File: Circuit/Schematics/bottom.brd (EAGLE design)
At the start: 38.1 x 38.1 mm, 52 parts, among them IC1 LM2936MP-3.3, Y1 16 Mhz, Y2 16 Mhz

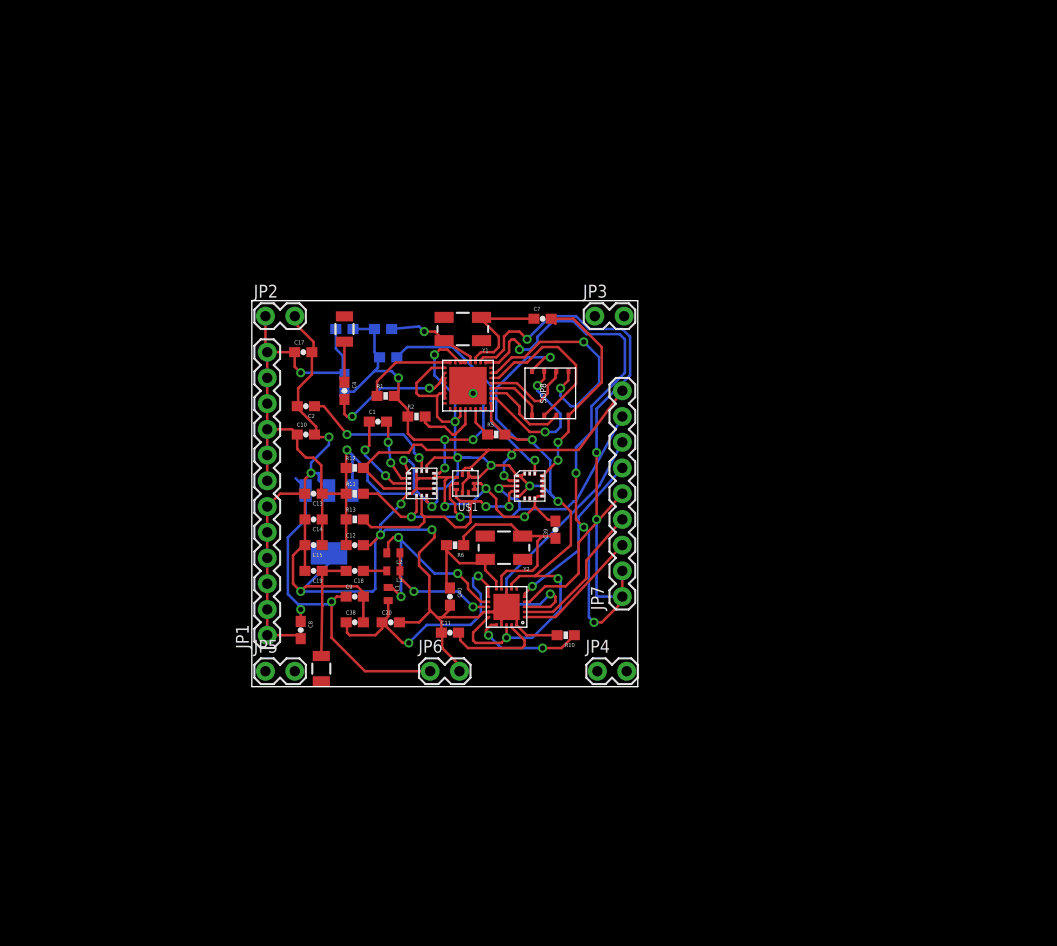
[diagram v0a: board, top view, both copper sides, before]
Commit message: P1 preliminary boards finished
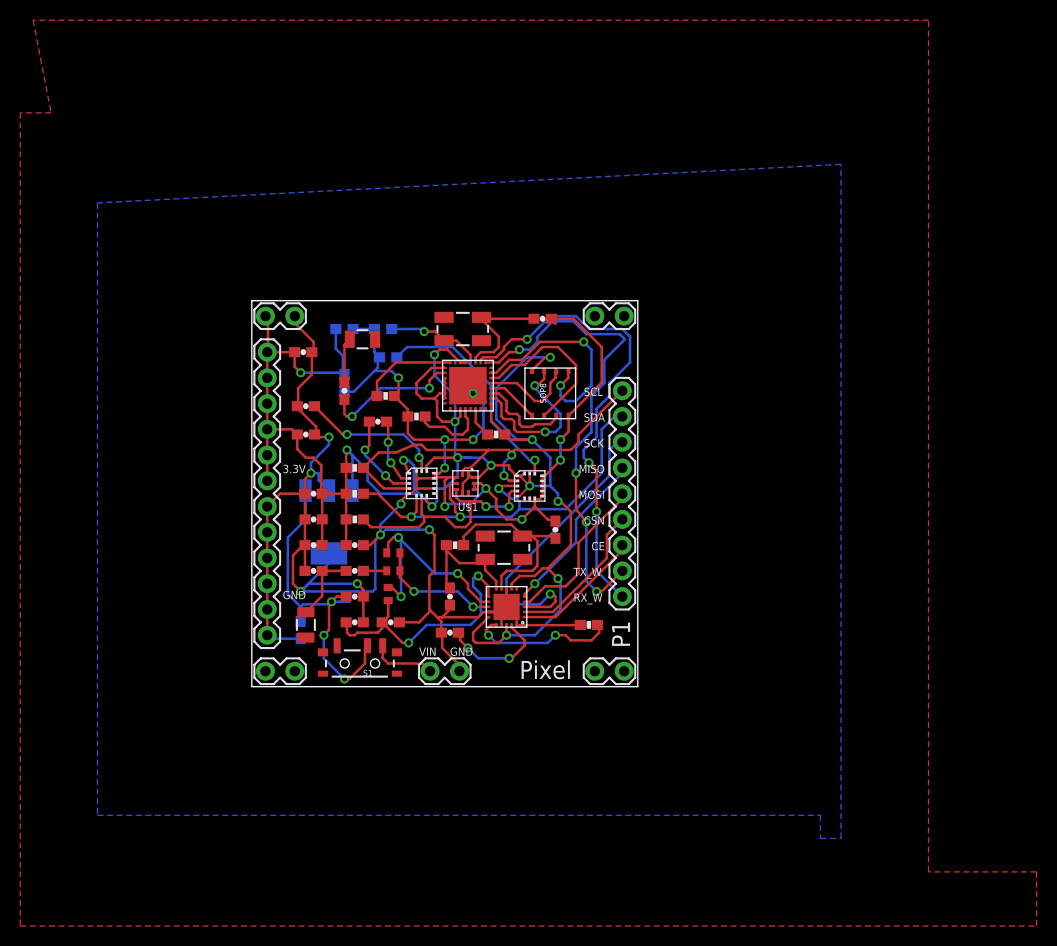
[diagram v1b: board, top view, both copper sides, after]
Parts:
- added S1: (no value), SparkFun-Electromechanical:SWITCH-SPST-SMD-A
- R11, R12, R13: value (none) -> 10k
- moved U$10 4.58 mm to (5.33, 6.10)
- moved R10 2.50 mm to (33.3, 6.10)
- moved U$9 2.05 mm to (10.9, 34.3), turned to 90 degrees
- moved JP4 0.25 mm to (34.0, 1.52)
- flipped C8 to the bottom
- renumbered U$2 to LSM303D, U$3 to L3GD20H
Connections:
- new net VIN: JP6.1, S1.1
- net VRAW: now also S1.2; no longer JP6.1
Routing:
- net TX_W: track 55.6 -> 47.5 mm
- net VIN: track 0.00 -> 6.43 mm
- net N$10: track 10.8 -> 7.12 mm
- net N$24: track 11.4 -> 14.8 mm
- net RX_W: track 48.5 -> 46.9 mm
- net GND: track 228.7 -> 230.3 mm, vias 16 -> 17
- net SD-D2: track 15.2 -> 16.7 mm
- net VRAW: track 35.5 -> 34.1 mm, vias 2 -> 3
- net SD-D1: track 23.1 -> 21.7 mm
- net SDA: track 43.7 -> 44.7 mm
- net SD-D3: track 8.49 -> 9.44 mm
- net N$16: track 19.3 -> 20.3 mm
- net N$28: track 10.1 -> 11.0 mm, vias 0 -> 2
- net SCK: track 29.2 -> 29.8 mm
- net N$3: track 7.00 -> 7.65 mm
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- added copper zone on layer 1, net GND
- added copper zone on layer 16, net GND
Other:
- board text added: "3.3V"
- board text added: "CE"
- board text added: "CSN"
- board text added: "GND"
- board text added: "MISO"
- board text added: "MOSI"
- board text added: "P1"
- board text added: "Pixel"
- board text added: "RX_W"
- board text added: "SCK"
- board text added: "SCL"
- board text added: "SDA"
- board text added: "TX_W"
- board text added: "VIN"
